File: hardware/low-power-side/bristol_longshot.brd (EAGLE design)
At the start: 38 x 48.1 mm, 83 parts, among them Q1 NX2301P, U1 SAM_D20E, U10 ADP1607ACPZN-R7, U11 TPS73118DBVT, U12 74LVC1G04GW, U14 SIT1552, U16 SIT1552, U2 SI4461, U3 SE880, U4 SST25WF040BT-40I/NP, U5 TG-5006CJ, U6 TG-5006CJ, U7 ADM6823WYRJZ, U8 SN74LVC1G32DCKR, U9 MS5607-02BA03

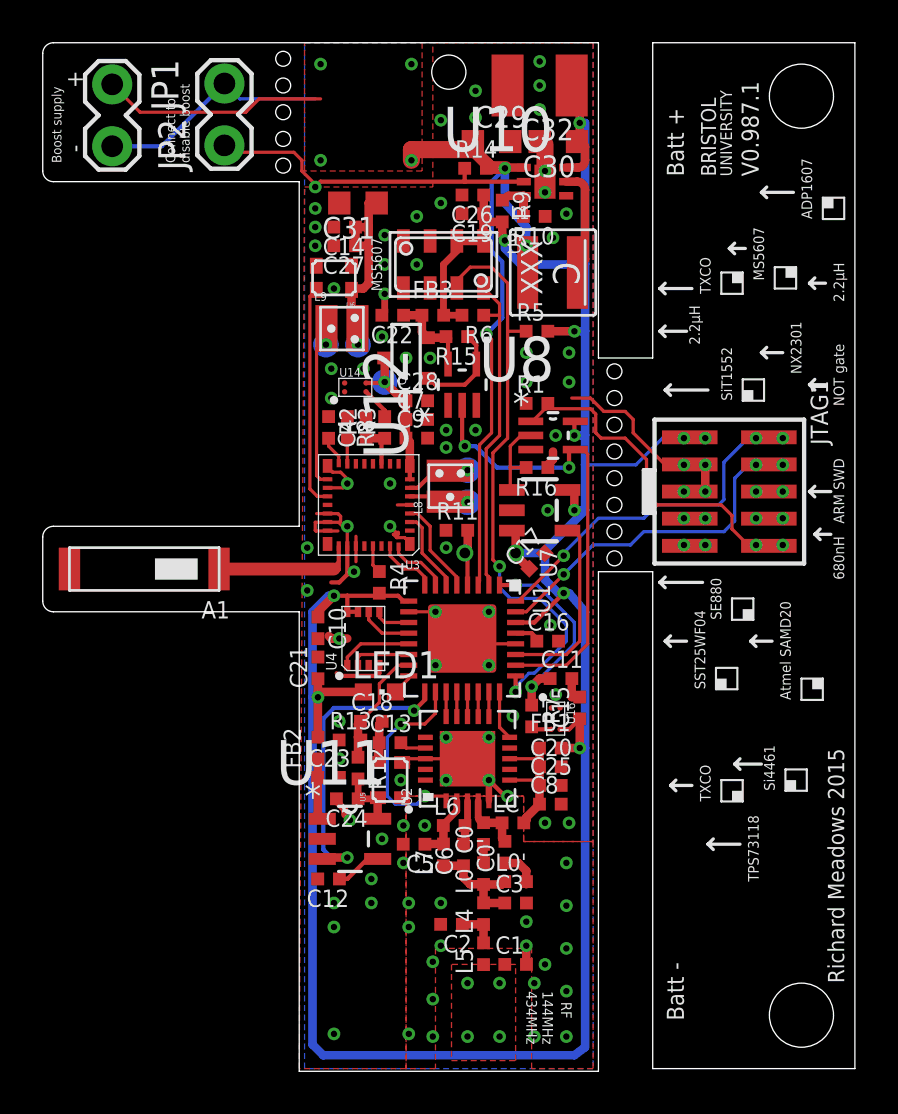
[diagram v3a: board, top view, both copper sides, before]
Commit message: [low-power] |v0.987.2|Low Power. Adjusted 100µF cap from 1210 to 1206
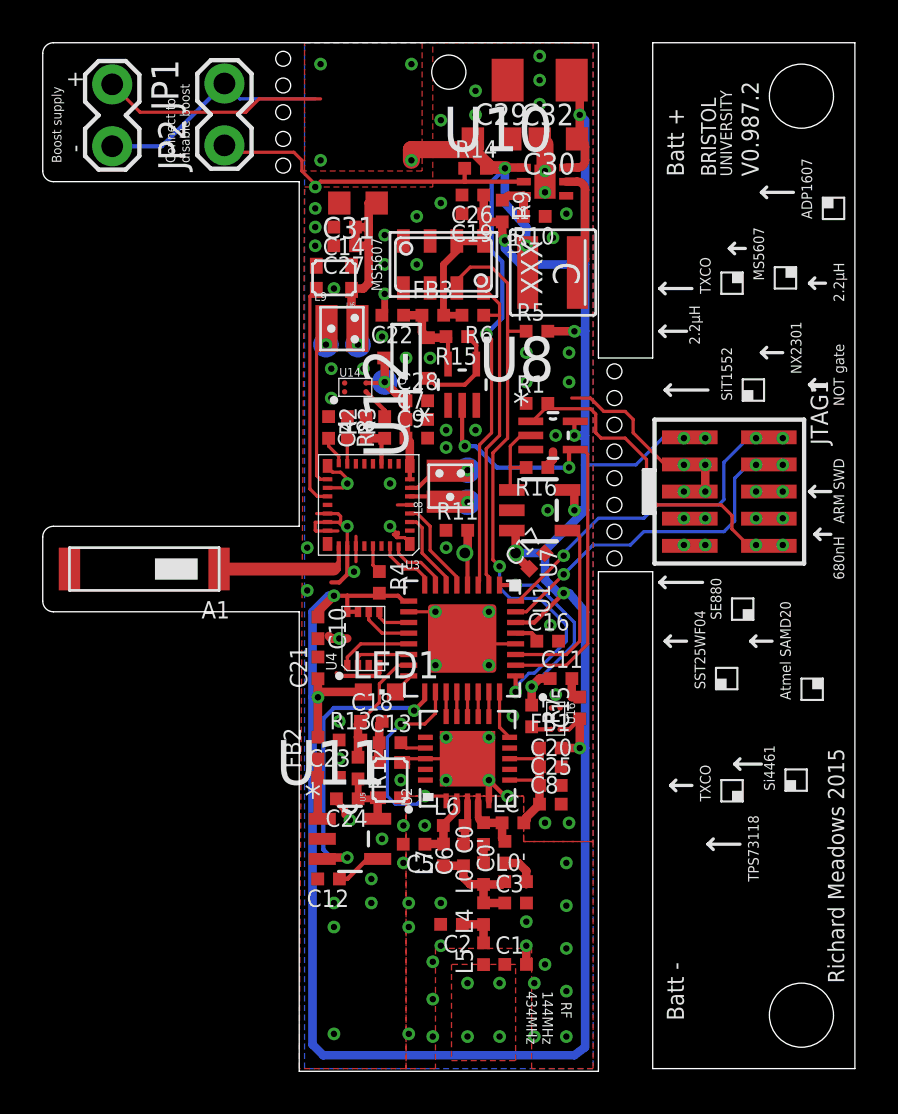
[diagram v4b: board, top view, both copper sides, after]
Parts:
- C32: device resistor:C1210K -> resistor:C1206K
- moved C32 0.25 mm to (23.2, 46.2)
- moved C29 0.12 mm to (21.0, 43.5)
- moved C30 0.12 mm to (24.1, 43.5)
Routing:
- net 1.8V: track 132.7 -> 133.3 mm
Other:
- board text added: "V0.987.2"
- board text removed: "V0.987.1"
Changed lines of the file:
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@@
 <?xml version="1.0" encoding="utf-8"?>
 <!DOCTYPE eagle SYSTEM "eagle.dtd">
-<eagle version="6.5.0">
+<eagle version="7.3.0">
 <drawing>
 <settings>
@@
 <layer number="23" name="tOrigins" color="15" fill="1" visible="yes" active="yes"/>
 <layer number="24" name="bOrigins" color="15" fill="1" visible="yes" active="yes"/>
-<layer number="25" name="tNames" color="7" fill="1" visible="yes" active="yes"/>
-<layer number="26" name="bNames" color="7" fill="1" visible="yes" active="yes"/>
-<layer number="27" name="tValues" color="7" fill="1" visible="yes" active="yes"/>
-<layer number="28" name="bValues" color="7" fill="1" visible="yes" active="yes"/>
+<layer number="25" name="tNames" color="7" fill="1" visible="no" active="yes"/>
+<layer number="26" name="bNames" color="7" fill="1" visible="no" active="yes"/>
+<layer number="27" name="tValues" color="7" fill="1" visible="no" active="yes"/>
+<layer number="28" name="bValues" color="7" fill="1" visible="no" active="yes"/>
 <layer number="29" name="tStop" color="7" fill="3" visible="yes" active="yes"/>
 <layer number="30" name="bStop" color="7" fill="6" visible="yes" active="yes"/>
@@
 <circle x="17.125" y="12.125" radius="0.1" width="0.2" layer="21"/>
 <rectangle x1="19.125" y1="0.375" x2="22.125" y2="4.75" layer="29"/>
-<text x="33.5" y="41.75" size="0.8" layer="21" font="vector" ratio="14" rot="R90">V0.987.1</text>
+<text x="33.5" y="41.75" size="0.8" layer="21" font="vector" ratio="14" rot="R90">V0.987.2</text>
 <text x="15.875" y="36.375" size="0.5" layer="21" font="vector" ratio="15" rot="SR90">MS5607</text>
 <text x="35" y="17.25" size="0.5" layer="21" font="vector" ratio="15" rot="SR90">Atmel SAMD20</text>
@@
 <pass name="Default">
 <param name="RoutingGrid" value="50mil"/>
+<param name="AutoGrid" value="1"/>
+<param name="Efforts" value="0"/>
+<param name="TopRouterVariant" value="1"/>
 <param name="tpViaShape" value="round"/>
 <param name="PrefDir.1" value="|"/>
@@
 <element name="R3" library="microbuilder_v3" package="_0402" value="10kΩ" x="14.25" y="30" rot="R270"/>
 <element name="R2" library="microbuilder_v3" package="_0402" value="10kΩ" x="13.375" y="30" rot="R270"/>
-<element name="C30" library="resistor" package="C0603K" value="10µF" x="24.125" y="43.375" rot="R180"/>
+<element name="C30" library="resistor" package="C0603K" value="10µF" x="24.125" y="43.5" rot="R180"/>
 <element name="U10" library="ADP1607" package="DFN200X200X60-7N" value="ADP1607ACPZN-R7" x="23.5" y="41.5">
 <attribute name="MPN" value="ADP1607ACPZN-R7" x="20.5" y="37.25" size="1.778" layer="27" display="off"/>
@@
 <element name="R9" library="microbuilder_v3" package="_0402" value="43kΩ" x="21.5" y="40.125" rot="R270"/>
 <element name="R10" library="microbuilder_v3" package="_0402" value="100kΩ" x="23" y="39.875" rot="R180"/>
-<element name="C29" library="resistor" package="C0603K" value="10µF" x="21" y="43.375"/>
+<element name="C29" library="resistor" package="C0603K" value="10µF" x="21" y="43.5"/>
 <element name="L1" library="Coilcraft_XAL" package="XFL4020" value="XFL4020-2.2µF" x="23.875" y="37.25"/>
 <element name="A1" library="1575AT43A40" package="1575AT43A40" value="1575AT43A40" x="4.75" y="23.375" rot="R180"/>
@@
 <element name="C23" library="microbuilder_v3" package="_0402" value="1µF" x="13.375" y="13.625"/>
 <element name="C12" library="microbuilder_v3" package="_0402" value="10nF" x="13.375" y="8.875" rot="R180"/>
-<element name="C32" library="resistor" package="C1210K" value="100µF" x="23.25" y="46" rot="R180"/>
 <element name="C10" library="microbuilder_v3" package="_0402" value="100pF" x="12.875" y="20.625" rot="R270"/>
 <element name="R11" library="microbuilder_v3" package="_0402" value="100kΩ" x="19.375" y="25.1875"/>
@@
 <element name="JP2" library="SparkFun" package="1X02_LOCK" value="" x="8.5" y="43.375" rot="R90"/>
 <element name="R16" library="microbuilder_v3" package="_0402" value="1MΩ" x="23.125" y="28.125" rot="R180"/>
+<element name="C32" library="resistor" package="C1206K" value="100µF" x="23.25" y="46.25" rot="R180"/>
 </elements>
 <signals>
@@
 <via x="14.375" y="11.625" extent="1-16" drill="0.3"/>
 <via x="23" y="4" extent="1-16" drill="0.3"/>
-<contactref element="C32" pad="2"/>
 <via x="13.625" y="36.5" extent="1-16" drill="0.3"/>
 <via x="12.75" y="40.25" extent="1-16" drill="0.3"/>
 <via x="16" y="39" extent="1-16" drill="0.3"/>
 <via x="20.25" y="45.75" extent="1-16" drill="0.3"/>
-<via x="20.25" y="44.5" extent="1-16" drill="0.3"/>
-<via x="23.25" y="46" extent="1-16" drill="0.3"/>
-<via x="23.25" y="44.875" extent="1-16" drill="0.3"/>
-<via x="23.25" y="47.125" extent="1-16" drill="0.3"/>
+<via x="20.25" y="44.625" extent="1-16" drill="0.3"/>
+<via x="23.25" y="46.25" extent="1-16" drill="0.3"/>
+<via x="23.25" y="45.125" extent="1-16" drill="0.3"/>
+<via x="23.25" y="47.375" extent="1-16" drill="0.3"/>
 <via x="13.625" y="6.625" extent="1-16" drill="0.3"/>
 <via x="17.125" y="6.625" extent="1-16" drill="0.3"/>
@@
 <wire x1="24.75" y1="18.25" x2="24.75" y2="17.383" width="0.4" layer="1"/>
 <wire x1="24.75" y1="17.383" x2="25.125" y2="17.383" width="0.4" layer="1"/>
+<contactref element="C32" pad="2"/>
 </signal>
 <signal name="SWDIO">
@@
 <wire x1="20.8125" y1="42.3125" x2="20.125" y2="43" width="0.6" layer="1"/>
 <wire x1="20.125" y1="43" x2="20.25" y2="43.25" width="0.6" layer="1"/>
-<wire x1="20.25" y1="43.25" x2="20.125" y2="43.375" width="0.6" layer="1"/>
+<wire x1="20.25" y1="43.25" x2="20.125" y2="43.5" width="0.6" layer="1"/>
 <wire x1="20.125" y1="43" x2="17.25" y2="43" width="0.8" layer="1"/>
 <wire x1="17.25" y1="43" x2="17.25" y2="42.5" width="0.8" layer="1"/>
@@
 <contactref element="U10" pad="6"/>
 <contactref element="R9" pad="2"/>
-<wire x1="25.1604" y1="43.3396" x2="25" y2="43.375" width="0.4" layer="1"/>
+<wire x1="25.1604" y1="43.3396" x2="25" y2="43.5" width="0.4" layer="1"/>
 <wire x1="24.4906" y1="42.1604" x2="25.0354" y2="42.1604" width="0.4" layer="1"/>
 <wire x1="25.0354" y1="42.1604" x2="25.375" y2="42.5" width="0.4" layer="1" curve="90"/>
 <wire x1="25.375" y1="42.5" x2="25.375" y2="43.125" width="0.4" layer="1"/>
-<wire x1="25.375" y1="43.125" x2="25" y2="43.375" width="0.4" layer="1" curve="90"/>
-<via x="25.125" y="44.25" extent="1-16" drill="0.3"/>
-<wire x1="25.375" y1="44.25" x2="25.125" y2="44.25" width="0.4" layer="16"/>
-<wire x1="25" y1="43.375" x2="25.125" y2="43.5" width="0.4" layer="1"/>
-<wire x1="25.125" y1="43.5" x2="25.125" y2="44.25" width="0.4" layer="1"/>
+<wire x1="25.375" y1="43.125" x2="25" y2="43.5" width="0.4" layer="1" curve="90"/>
+<via x="25.125" y="44.625" extent="1-16" drill="0.3"/>
+<wire x1="25.375" y1="44.375" x2="25.125" y2="44.625" width="0.4" layer="16"/>
+<wire x1="25" y1="43.5" x2="25.125" y2="43.5" width="0.4" layer="1"/>
+<wire x1="25.125" y1="43.5" x2="25.125" y2="44.625" width="0.4" layer="1"/>
 <via x="22.125" y="24.125" extent="1-16" drill="0.5"/>
 <via x="21.625" y="38.75" extent="1-16" drill="0.3"/>
-<wire x1="25.375" y1="44.25" x2="25.375" y2="37.625" width="0.4" layer="16"/>
+<wire x1="25.375" y1="44.375" x2="25.375" y2="37.625" width="0.4" layer="16"/>
 <wire x1="25.375" y1="37.625" x2="25.375" y2="34.5" width="0.4" layer="16"/>
 <wire x1="25.375" y1="34.5" x2="25.375" y2="29.625" width="0.4" layer="16"/>
@@
 <wire x1="24.875" y1="0.625" x2="25.375" y2="1" width="0.4" layer="16"/>
 <wire x1="25.375" y1="1" x2="25.375" y2="15" width="0.4" layer="16"/>
-<contactref element="C32" pad="1"/>
 <wire x1="25.375" y1="15" x2="25.375" y2="21.375" width="0.4" layer="16"/>
-<wire x1="25.125" y1="44.25" x2="25.125" y2="46" width="0.4" layer="1"/>
-<wire x1="25.125" y1="46" x2="24.75" y2="46" width="0.4" layer="1"/>
+<wire x1="25.125" y1="44.625" x2="25.125" y2="46" width="0.4" layer="1"/>
 <wire x1="25.375" y1="28.25" x2="27.75" y2="28.25" width="0.1524" layer="16"/>
 <wire x1="27.75" y1="28.25" x2="29" y2="29.5" width="0.1524" layer="16"/>
@@
 <wire x1="30.275" y1="29.54" x2="30.04" y2="29.54" width="0.4" layer="1"/>
 <wire x1="30.04" y1="29.54" x2="30" y2="29.5" width="0.4" layer="1"/>
+<contactref element="C32" pad="1"/>
+<wire x1="25.125" y1="46" x2="24.75" y2="46" width="0.2" layer="1"/>
+<wire x1="24.75" y1="46" x2="24.75" y2="46.25" width="0.2" layer="1"/>
 </signal>
 <signal name="MEM_WPN">
@@
 <contactref element="R7" pad="1"/>
 <contactref element="C11" pad="1"/>
-<wire x1="22.875" y1="17.883" x2="22.875" y2="17.008" width="0.4" layer="1"/>
+<wire x1="22.875" y1="17.883" x2="22.875" y2="17.875" width="0.4" layer="1"/>
+<wire x1="22.875" y1="17.875" x2="22.875" y2="17.008" width="0.4" layer="1"/>
 <wire x1="22.875" y1="17.883" x2="23.242" y2="18.25" width="0.4" layer="1"/>
 <wire x1="23.242" y1="18.25" x2="23.742" y2="18.25" width="0.4" layer="1"/>
@@
 <wire x1="24.875" y1="20.875" x2="24.875" y2="19.875" width="0.1524" layer="16"/>
 <wire x1="24.875" y1="19.875" x2="22.875" y2="17.875" width="0.1524" layer="16"/>
-<wire x1="22.875" y1="17.883" x2="22.875" y2="17.875" width="0" layer="19" extent="1-1"/>
 </signal>
 <signal name="LF_CLOCK_OUT">
